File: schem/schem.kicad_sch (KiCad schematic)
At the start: 7 parts, among them SW1 SW_SPST, SW2 SW_DIP_x01, U1 ProMicro, U2 CD74HC4067M, U3 ADS7885, U4 CD74HC4067M, U5 OH49E-S

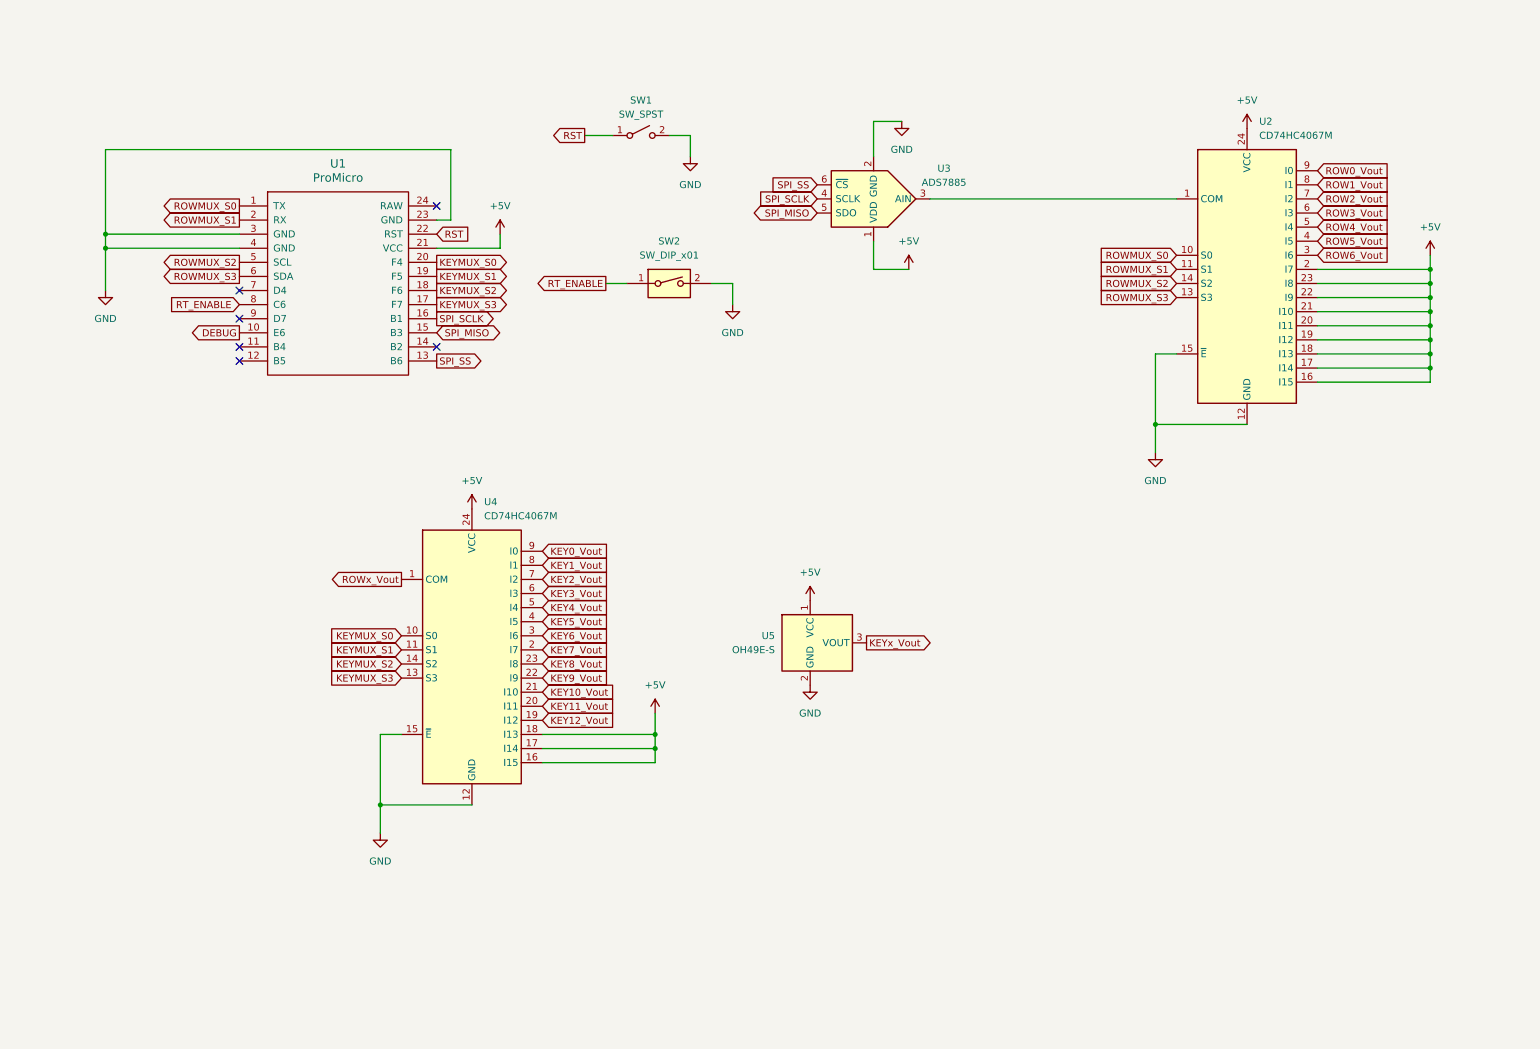
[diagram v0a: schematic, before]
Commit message: Optimize SPI read routine with inline asm
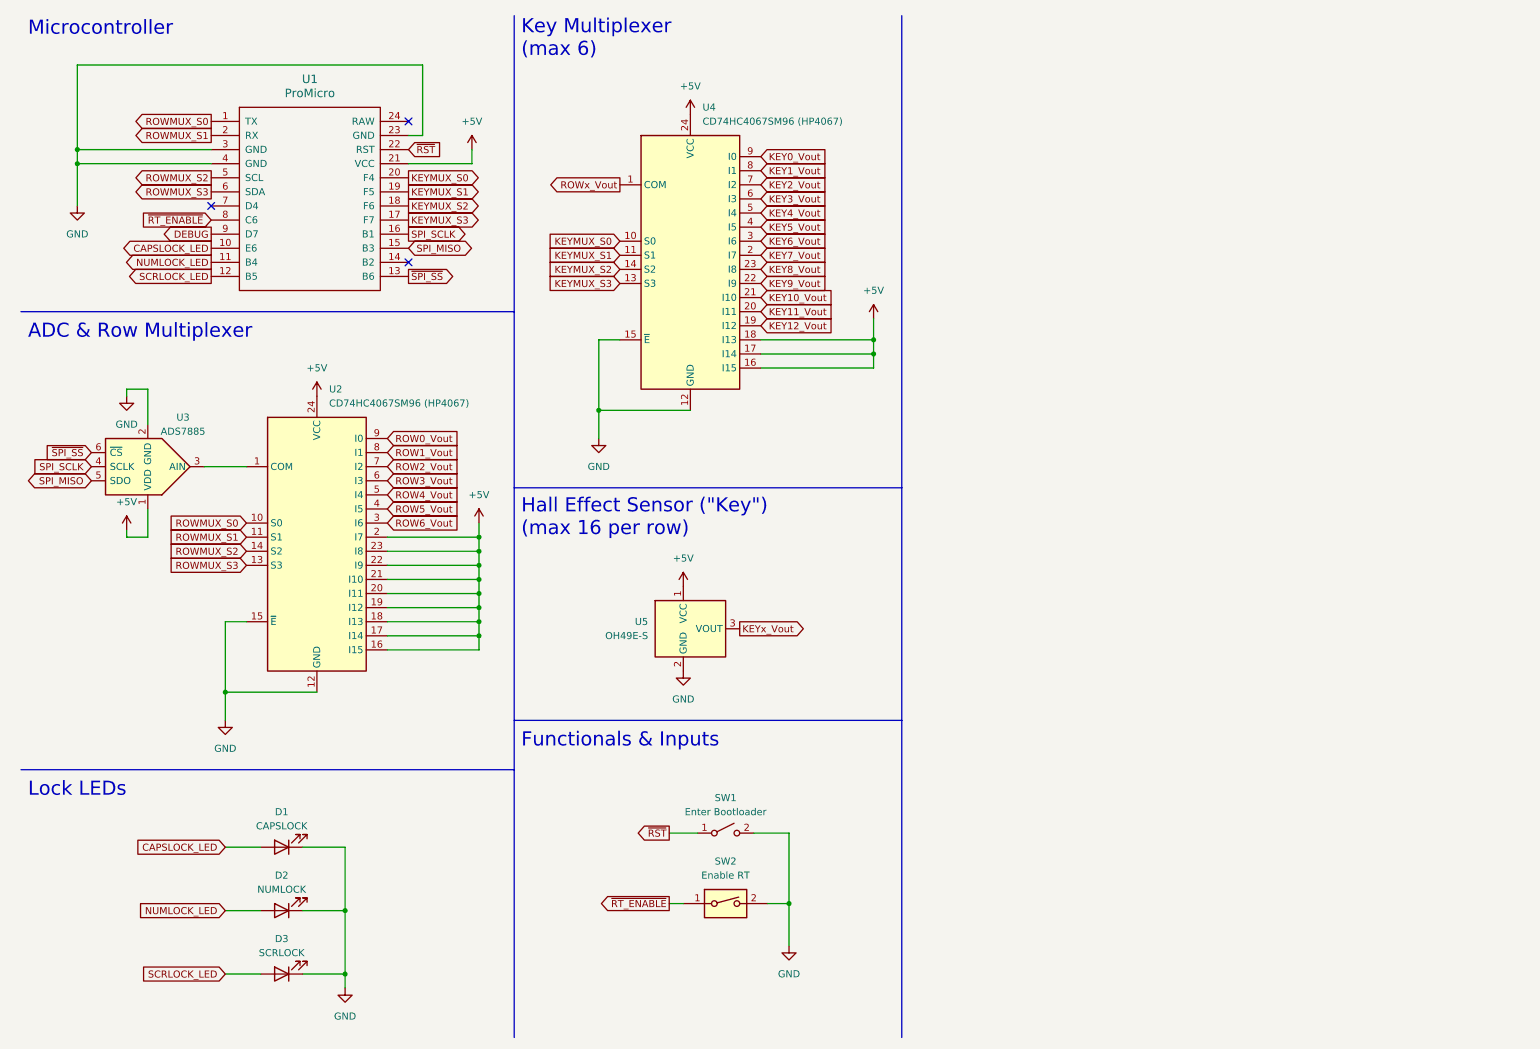
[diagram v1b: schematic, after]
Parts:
- added D1: CAPSLOCK, symbol Device:LED
- added D2: NUMLOCK, symbol Device:LED
- added D3: SCRLOCK, symbol Device:LED
- SW1: value SW_SPST -> Enter Bootloader
- SW2: value SW_DIP_x01 -> Enable RT
- U2, U4: value CD74HC4067M -> CD74HC4067SM96 (HP4067)
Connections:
- net DEBUG: now also U1.9 (D7); no longer U1.10 (E6)
- net GND: now also D1.1 (K), D2.1 (K), D3.1 (K)
- net NUMLOCK_LED: now reaches U1.11 (B4)
- net NUMLOCK_LED: now also D2.2 (A)
- net SCRLOCK_LED: now reaches U1.12 (B5)
- net SCRLOCK_LED: now also D3.2 (A)
- net RST renamed ~{RST}
- net RT_ENABLE renamed ~{RT_ENABLE}
- net SPI_SS renamed ~{SPI_SS}
- new net CAPSLOCK_LED: D1.2 (A), U1.10 (E6)
- no-connect marks 6 -> 3
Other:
- note added: "ADC & Row Multiplexer"
- note added: "Functionals & Inputs"
- note added: "Hall Effect Sensor ("Key") (max 16 per row)"
- note added: "Key Multiplexer (max 6)"
- note added: "Lock LEDs"
- note added: "Microcontroller"
- moved on the sheet: U1, U2, U3, U4, U5

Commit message: Add rotary encoder to and remove RT switch from schematic
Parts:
- removed SW2: Enable RT, symbol Switch:SW_DIP_x01
- added R1, R2, R3: 10k, symbol Device:R_US
- added SW3: RotaryEncoder_Switch, symbol Device:RotaryEncoder_Switch
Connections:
- net +5V: now also R1.2, R2.2, R3.2
- net GND: now also SW3.C, SW3.S1
- net ROTENC_CLK: now reaches U1.7 (D4)
- net ROTENC_CLK: now also R1.1, SW3.A
- net DEBUG renamed ROTENC_DT
- net ROTENC_DT: now also R2.1, SW3.B
- net ~{RT_ENABLE} renamed ROTENC_SW
- net ROTENC_SW: now also R3.1, SW3.S2
- no-connect marks 3 -> 2
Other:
- note added: "Rotary Encoder"
- moved on the sheet: SW1
